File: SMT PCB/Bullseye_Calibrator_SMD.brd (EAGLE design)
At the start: 50.8 x 66 mm, 16 parts

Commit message: Add files via upload
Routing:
- net S$57: track 42.3 -> 33.8 mm, vias 2 -> 0
- net S$64: track 0.00 -> 8.26 mm
- net S$46: vias 1 -> 0
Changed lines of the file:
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@@
 <layer number="21" name="tPlace" color="7" fill="1" visible="yes" active="yes"/>
 <layer number="22" name="bPlace" color="7" fill="1" visible="yes" active="yes"/>
-<layer number="23" name="tOrigins" color="15" fill="1" visible="yes" active="yes"/>
-<layer number="24" name="bOrigins" color="15" fill="1" visible="yes" active="yes"/>
+<layer number="23" name="tOrigins" color="15" fill="1" visible="no" active="yes"/>
+<layer number="24" name="bOrigins" color="15" fill="1" visible="no" active="yes"/>
 <layer number="25" name="tNames" color="7" fill="1" visible="yes" active="yes"/>
 <layer number="26" name="bNames" color="7" fill="1" visible="yes" active="yes"/>
 <layer number="27" name="tValues" color="7" fill="1" visible="yes" active="yes"/>
 <layer number="28" name="bValues" color="7" fill="1" visible="yes" active="yes"/>
-<layer number="29" name="tStop" color="7" fill="3" visible="yes" active="yes"/>
-<layer number="30" name="bStop" color="7" fill="6" visible="yes" active="yes"/>
-<layer number="31" name="tCream" color="7" fill="4" visible="yes" active="yes"/>
-<layer number="32" name="bCream" color="7" fill="5" visible="yes" active="yes"/>
+<layer number="29" name="tStop" color="7" fill="3" visible="no" active="yes"/>
+<layer number="30" name="bStop" color="7" fill="6" visible="no" active="yes"/>
+<layer number="31" name="tCream" color="7" fill="4" visible="no" active="yes"/>
+<layer number="32" name="bCream" color="7" fill="5" visible="no" active="yes"/>
 <layer number="33" name="tFinish" color="6" fill="3" visible="yes" active="yes"/>
 <layer number="34" name="bFinish" color="6" fill="6" visible="yes" active="yes"/>
@@
 <wire x1="37.626753125" y1="43.18" x2="33.02" y2="43.18" width="0.8128" layer="1"/>
 </signal>
+<signal name="S$66">
+<wire x1="10.18568125" y1="35.56" x2="10.16" y2="35.56" width="1.778" layer="16"/>
+</signal>
 <signal name="S$46">
 <wire x1="43.6577875" y1="45.67815" x2="43.6577875" y2="39.2058875" width="1.4224" layer="1"/>
 <wire x1="43.6577875" y1="39.2058875" x2="10.18568125" y2="39.2058875" width="1.4224" layer="1"/>
 <wire x1="10.18568125" y1="39.2058875" x2="10.18568125" y2="35.56" width="1.4224" layer="1"/>
-<wire x1="10.18568125" y1="35.56" x2="10.16" y2="35.56" width="1.778" layer="16"/>
-<via x="10.18568125" y="35.56" extent="1-16" drill="0.6" shape="square"/>
-</signal>
-<signal name="S$57">
+</signal>
+<signal name="S$64">
 <wire x1="21.175271875" y1="54.165178125" x2="21.175271875" y2="62.4286" width="1.6764" layer="1"/>
+</signal>
+<signal name="S$65">
 <wire x1="21.175271875" y1="62.4286" x2="21.25105625" y2="62.4286" width="1.6764" layer="16"/>
 <wire x1="21.25105625" y1="62.4286" x2="21.25105625" y2="62.314884375" width="1.6764" layer="16"/>
+</signal>
+<signal name="S$57">
 <wire x1="21.25105625" y1="62.314884375" x2="29.246228125" y2="62.314884375" width="1.6764" layer="1"/>
 <wire x1="29.246228125" y1="62.314884375" x2="29.246228125" y2="54.09108125" width="1.6764" layer="1"/>
 <wire x1="29.246228125" y1="54.09108125" x2="43.2274" y2="54.09108125" width="1.4224" layer="1"/>
 <wire x1="43.2274" y1="54.09108125" x2="43.2274" y2="50.442665625" width="1.4224" layer="1"/>
-<via x="21.25105625" y="62.314884375" extent="1-16" drill="0.6" shape="square"/>
-<via x="21.175271875" y="62.4286" extent="1-16" drill="0.6" shape="square"/>
 </signal>
 <signal name="S$43">

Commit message: Add files via upload
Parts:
- added J3: (no value), jumper:JP1
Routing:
- net S$71: track 0.00 -> 29.6 mm
- net S$70: track 0.00 -> 24.5 mm
- net S$67: track 0.00 -> 16.2 mm
- net S$57: track 33.8 -> 23.1 mm
- net S$69: track 0.00 -> 8.06 mm
- net S$68: track 0.00 -> 3.07 mm
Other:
- board text added: "25 MHz Out"
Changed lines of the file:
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@@
 <layer number="21" name="tPlace" color="7" fill="1" visible="yes" active="yes"/>
 <layer number="22" name="bPlace" color="7" fill="1" visible="yes" active="yes"/>
-<layer number="23" name="tOrigins" color="15" fill="1" visible="no" active="yes"/>
-<layer number="24" name="bOrigins" color="15" fill="1" visible="no" active="yes"/>
+<layer number="23" name="tOrigins" color="15" fill="1" visible="yes" active="yes"/>
+<layer number="24" name="bOrigins" color="15" fill="1" visible="yes" active="yes"/>
 <layer number="25" name="tNames" color="7" fill="1" visible="yes" active="yes"/>
 <layer number="26" name="bNames" color="7" fill="1" visible="yes" active="yes"/>
 <layer number="27" name="tValues" color="7" fill="1" visible="yes" active="yes"/>
 <layer number="28" name="bValues" color="7" fill="1" visible="yes" active="yes"/>
-<layer number="29" name="tStop" color="7" fill="3" visible="no" active="yes"/>
-<layer number="30" name="bStop" color="7" fill="6" visible="no" active="yes"/>
-<layer number="31" name="tCream" color="7" fill="4" visible="no" active="yes"/>
-<layer number="32" name="bCream" color="7" fill="5" visible="no" active="yes"/>
+<layer number="29" name="tStop" color="7" fill="3" visible="yes" active="yes"/>
+<layer number="30" name="bStop" color="7" fill="6" visible="yes" active="yes"/>
+<layer number="31" name="tCream" color="7" fill="4" visible="yes" active="yes"/>
+<layer number="32" name="bCream" color="7" fill="5" visible="yes" active="yes"/>
 <layer number="33" name="tFinish" color="6" fill="3" visible="yes" active="yes"/>
 <layer number="34" name="bFinish" color="6" fill="6" visible="yes" active="yes"/>
@@
 G4EML</text>
 <text x="14.365821875" y="26.578703125" size="1.778" layer="21" font="fixed">ARDUINO NANO</text>
+<text x="42.65035" y="60.322175" size="1.778" layer="21" align="center">25
+MHz
+Out</text>
 </plain>
 <attributes>
@@
 <attribute name="VALUE" x="12.406625" y="49.139590625" size="1.27" layer="27" rot="R270"/>
 </element>
+<element name="J3" library="jumper" package="JP1" value="" x="46.93469375" y="59.850865625" smashed="yes">
+<attribute name="NAME" x="48.02838125" y="64.295721875" size="1.27" layer="25" ratio="10" rot="R180"/>
+<attribute name="VALUE" x="49.85569375" y="57.310865625" size="1.27" layer="27" ratio="10" rot="R90"/>
+</element>
 </elements>
 <signals>
@@
 <wire x1="21.25105625" y1="62.4286" x2="21.25105625" y2="62.314884375" width="1.6764" layer="16"/>
 </signal>
-<signal name="S$57">
+<signal name="S$67">
 <wire x1="21.25105625" y1="62.314884375" x2="29.246228125" y2="62.314884375" width="1.6764" layer="1"/>
 <wire x1="29.246228125" y1="62.314884375" x2="29.246228125" y2="54.09108125" width="1.6764" layer="1"/>
-<wire x1="29.246228125" y1="54.09108125" x2="43.2274" y2="54.09108125" width="1.4224" layer="1"/>
-<wire x1="43.2274" y1="54.09108125" x2="43.2274" y2="50.442665625" width="1.4224" layer="1"/>
+</signal>
+<signal name="S$57">
+<wire x1="29.246228125" y1="54.09108125" x2="43.7092375" y2="54.069178125" width="1.4224" layer="16"/>
+<wire x1="43.7092375" y1="54.069178125" x2="43.7358625" y2="45.4348" width="1.4224" layer="16"/>
 </signal>
 <signal name="S$43">
@@
 <wire x1="25.4" y1="48.6216125" x2="25.403265625" y2="48.6216125" width="0.8128" layer="1"/>
 </signal>
+<signal name="S$68">
+<wire x1="40.64594375" y1="50.511465625" x2="43.717578125" y2="50.511465625" width="1.4224" layer="16"/>
+</signal>
+<signal name="S$69">
+<wire x1="46.984446875" y1="58.63309375" x2="46.98445" y2="54.15151875" width="1.4224" layer="16"/>
+<wire x1="46.98445" y1="54.15151875" x2="43.411159375" y2="54.060634375" width="1.4224" layer="16"/>
+</signal>
+<signal name="S$70">
+<wire x1="29.198825" y1="54.139325" x2="29.198825" y2="62.30840625" width="1.6764" layer="16"/>
+<wire x1="29.198825" y1="62.30840625" x2="21.116028125" y2="62.30840625" width="1.6764" layer="16"/>
+<wire x1="21.116028125" y1="62.30840625" x2="21.116028125" y2="54.117425" width="1.6764" layer="16"/>
+<wire x1="21.116028125" y1="54.117425" x2="21.137934375" y2="54.117425" width="1.4224" layer="16"/>
+</signal>
+<signal name="S$71">
+<wire x1="29.894465625" y1="48.64216875" x2="29.894465625" y2="50.54755625" width="0.8128" layer="1"/>
+<wire x1="29.894465625" y1="50.54755625" x2="32.982465625" y2="50.54755625" width="0.8128" layer="1"/>
+<wire x1="32.982465625" y1="50.54755625" x2="32.982465625" y2="61.069878125" width="0.8128" layer="1"/>
+<wire x1="32.982465625" y1="61.069878125" x2="47.107109375" y2="61.06988125" width="0.8128" layer="1"/>
+</signal>
 </signals>

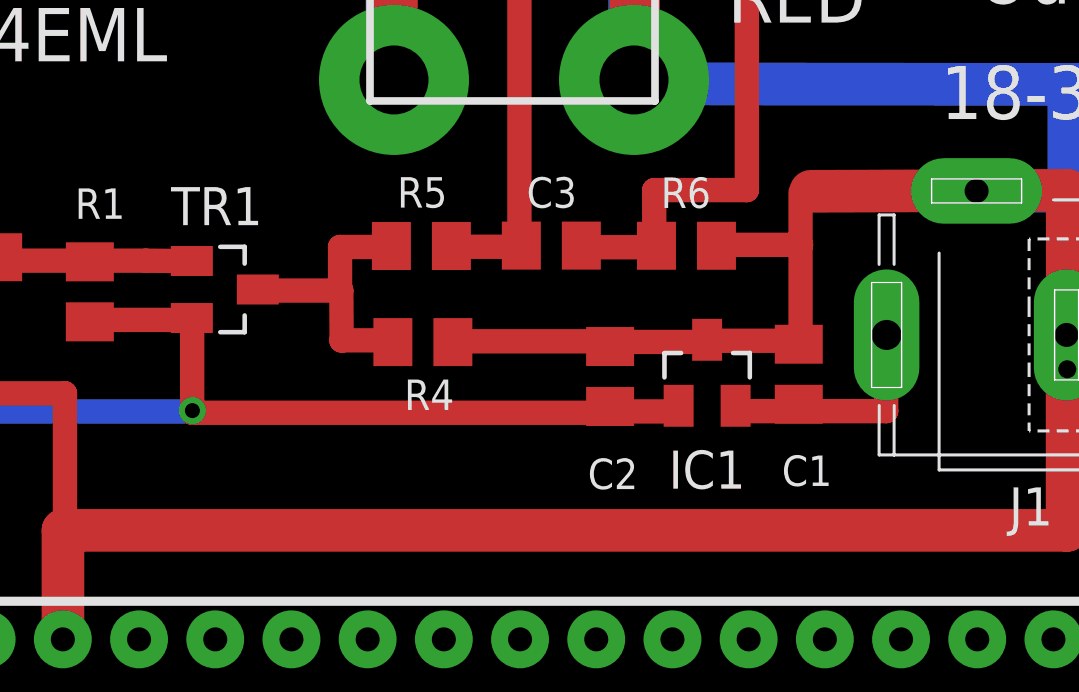
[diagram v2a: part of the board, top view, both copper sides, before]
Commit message: Add Input Diode
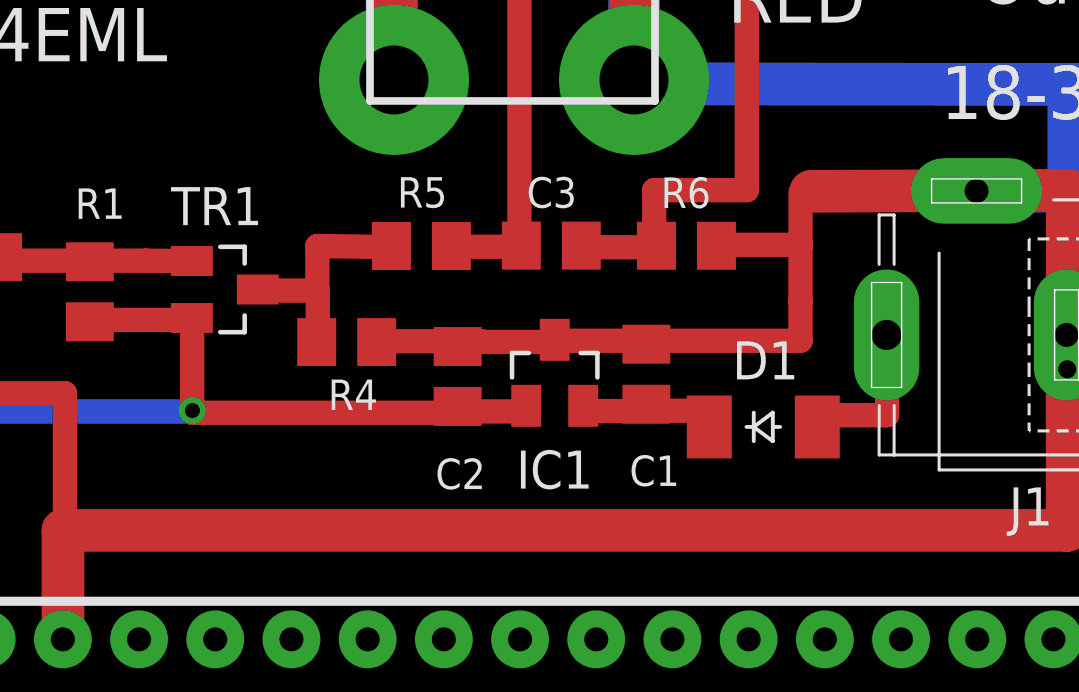
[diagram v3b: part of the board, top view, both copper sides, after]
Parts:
- added D1: (no value), diode:SOD-123_MINI-SMA
- moved C1 5.08 mm to (29.6, 44.4)
- moved C2 5.08 mm to (23.3, 44.3)
- moved IC1 5.08 mm to (26.6, 44.5)
- moved R4 2.54 mm to (19.6, 45.5)
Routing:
- net S$52: track 20.5 -> 15.5 mm
- net S$56: track 5.54 -> 0.46 mm
- net S$43: track 8.08 -> 13.2 mm
- net S$72: track 0.00 -> 4.58 mm
- net S$45: track 7.16 -> 3.97 mm
- net S$58: track 1.53 -> 3.16 mm
- net S$55: track 4.36 -> 3.57 mm
- net S$59: track 3.09 -> 3.85 mm
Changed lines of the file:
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@@
 <attribute name="VALUE" x="12.980653125" y="46.15735625" size="1.016" layer="27" rot="R90"/>
 </element>
-<element name="R4" library="resistor" package="C0805K" value="" x="22.182725" y="45.481446875" smashed="yes" rot="R180">
-<attribute name="NAME" x="23.22906875" y="44.235890625" size="1.016" layer="25" rot="R180"/>
-<attribute name="VALUE" x="23.182725" y="47.381446875" size="1.016" layer="27" rot="R180"/>
+<element name="R4" library="resistor" package="C0805K" value="" x="19.642725" y="45.481446875" smashed="yes" rot="R180">
+<attribute name="NAME" x="20.68906875" y="44.235890625" size="1.016" layer="25" rot="R180"/>
+<attribute name="VALUE" x="20.642725" y="47.381446875" size="1.016" layer="27" rot="R180"/>
 </element>
 <element name="R2" library="resistor" package="C0805K" value="" x="7.17551875" y="48.310884375" smashed="yes">
@@
 <attribute name="VALUE" x="6.98" y="39.64" size="1.016" layer="27" rot="R90"/>
 </element>
-<element name="C2" library="resistor" package="C0805K" value="" x="28.4231375" y="44.334334375" smashed="yes" rot="R90">
-<attribute name="NAME" x="29.352946875" y="41.598025" size="1.016" layer="25" rot="R180"/>
-<attribute name="VALUE" x="30.3231375" y="43.334334375" size="1.016" layer="27" rot="R90"/>
-</element>
-<element name="C1" library="resistor" package="C0805K" value="" x="34.712721875" y="44.41035625" smashed="yes" rot="R90">
-<attribute name="NAME" x="35.8213625" y="41.70223125" size="1.016" layer="25" rot="R180"/>
-<attribute name="VALUE" x="36.612721875" y="43.41035625" size="1.016" layer="27" rot="R90"/>
-</element>
-<element name="IC1" library="avago" package="SOT23" value="" x="31.65776875" y="44.457725" smashed="yes">
-<attribute name="NAME" x="30.377315625" y="40.59605625" size="1.27" layer="25"/>
-<attribute name="VALUE" x="29.75276875" y="41.282725" size="1.27" layer="27"/>
+<element name="C2" library="resistor" package="C0805K" value="" x="23.3431375" y="44.334334375" smashed="yes" rot="R90">
+<attribute name="NAME" x="24.272946875" y="41.598025" size="1.016" layer="25" rot="R180"/>
+<attribute name="VALUE" x="25.2431375" y="43.334334375" size="1.016" layer="27" rot="R90"/>
+</element>
+<element name="C1" library="resistor" package="C0805K" value="" x="29.632721875" y="44.41035625" smashed="yes" rot="R90">
+<attribute name="NAME" x="30.7413625" y="41.70223125" size="1.016" layer="25" rot="R180"/>
+<attribute name="VALUE" x="31.532721875" y="43.41035625" size="1.016" layer="27" rot="R90"/>
+</element>
+<element name="IC1" library="avago" package="SOT23" value="" x="26.57776875" y="44.457725" smashed="yes">
+<attribute name="NAME" x="25.297315625" y="40.59605625" size="1.27" layer="25"/>
+<attribute name="VALUE" x="24.67276875" y="41.282725" size="1.27" layer="27"/>
 </element>
 <element name="TR2" library="avago" package="SOT23" value="" x="6.06380625" y="44.914759375" smashed="yes">
@@
 <attribute name="NAME" x="48.02838125" y="64.295721875" size="1.27" layer="25" ratio="10" rot="R180"/>
 <attribute name="VALUE" x="49.85569375" y="57.310865625" size="1.27" layer="27" ratio="10" rot="R90"/>
+</element>
+<element name="D1" library="diode" package="SOD-123_MINI-SMA" value="" x="33.529925" y="42.65389375" smashed="yes">
+<attribute name="NAME" x="32.500659375" y="44.238575" size="1.27" layer="25"/>
+<attribute name="VALUE" x="30.481925" y="40.24089375" size="1.27" layer="27"/>
 </element>
 </elements>
@@
 </signal>
 <signal name="S$45">
-<wire x1="37.626753125" y1="45.73158125" x2="37.626753125" y2="43.18" width="0.8128" layer="1"/>
-<wire x1="37.626753125" y1="43.18" x2="33.02" y2="43.18" width="0.8128" layer="1"/>
+<wire x1="31.913771875" y1="43.198246875" x2="27.94" y2="43.18" width="0.8128" layer="1"/>
 </signal>
 <signal name="S$66">
@@
 </signal>
 <signal name="S$43">
-<wire x1="31.64364375" y1="45.525934375" x2="34.771325" y2="45.525934375" width="0.8128" layer="1"/>
-<wire x1="34.771325" y1="45.525934375" x2="34.771325" y2="50.47855625" width="0.8128" layer="1"/>
+<wire x1="26.56364375" y1="45.525934375" x2="34.770703125" y2="45.525934375" width="0.8128" layer="1"/>
+<wire x1="34.770703125" y1="45.525934375" x2="34.770703125" y2="46.839978125" width="0.8128" layer="1"/>
+<wire x1="34.770703125" y1="46.839978125" x2="34.771325" y2="50.47855625" width="0.8128" layer="1"/>
 </signal>
 <signal name="S$47">
-<wire x1="31.717871875" y1="45.4873375" x2="28.300915625" y2="45.4873375" width="0.8128" layer="1"/>
+<wire x1="26.637871875" y1="45.4873375" x2="23.220915625" y2="45.4873375" width="0.8128" layer="1"/>
 </signal>
 <signal name="S$48">
-<wire x1="30.6754125" y1="43.171478125" x2="28.455353125" y2="43.171478125" width="0.8128" layer="1"/>
-<wire x1="28.455353125" y1="43.171478125" x2="28.455353125" y2="43.152178125" width="0.8128" layer="1"/>
+<wire x1="25.5954125" y1="43.171478125" x2="23.375353125" y2="43.171478125" width="0.8128" layer="1"/>
+<wire x1="23.375353125" y1="43.171478125" x2="23.375353125" y2="43.152178125" width="0.8128" layer="1"/>
 </signal>
 <signal name="S$34">
@@
 <wire x1="11.099271875" y1="46.221234375" x2="14.493153125" y2="46.221234375" width="0.8128" layer="1"/>
 <wire x1="14.493153125" y1="46.221234375" x2="14.493153125" y2="43.1259125" width="0.8128" layer="1"/>
-<wire x1="14.493153125" y1="43.1259125" x2="28.50586875" y2="43.1259125" width="0.8128" layer="1"/>
-<wire x1="28.50586875" y1="43.1259125" x2="28.50586875" y2="43.165953125" width="0.8128" layer="1"/>
+<wire x1="14.493153125" y1="43.1259125" x2="23.42586875" y2="43.1259125" width="0.8128" layer="1"/>
+<wire x1="23.42586875" y1="43.1259125" x2="23.42586875" y2="43.165953125" width="0.8128" layer="1"/>
 </signal>
 <signal name="S$53">
@@
 </signal>
 <signal name="S$55">
-<wire x1="16.775975" y1="47.199303125" x2="19.4638375" y2="47.199303125" width="0.8128" layer="1"/>
-<wire x1="19.4638375" y1="47.199303125" x2="19.475003125" y2="45.530175" width="0.8128" layer="1"/>
+<wire x1="16.775975" y1="47.199303125" x2="18.67516875" y2="47.199303125" width="0.8128" layer="1"/>
+<wire x1="18.67516875" y1="47.199303125" x2="18.686334375" y2="45.530175" width="0.8128" layer="1"/>
 </signal>
 <signal name="S$56">
-<wire x1="23.2327375" y1="45.508721875" x2="28.512196875" y2="45.50871875" width="0.8128" layer="1"/>
-<wire x1="28.512196875" y1="45.50871875" x2="28.454278125" y2="45.25389375" width="0.8128" layer="1"/>
+<wire x1="23.2327375" y1="45.508721875" x2="23.432196875" y2="45.50871875" width="0.8128" layer="1"/>
+<wire x1="23.432196875" y1="45.50871875" x2="23.374278125" y2="45.25389375" width="0.8128" layer="1"/>
 </signal>
 <signal name="S$58">
-<wire x1="19.462446875" y1="45.540190625" x2="20.990490625" y2="45.540190625" width="0.8128" layer="1"/>
+<wire x1="24.146146875" y1="45.509778125" x2="20.990490625" y2="45.509778125" width="0.8128" layer="1"/>
 </signal>
 <signal name="S$59">
-<wire x1="19.42208125" y1="47.147034375" x2="19.42208125" y2="48.65234375" width="0.8128" layer="1"/>
-<wire x1="19.42208125" y1="48.65234375" x2="21.00519375" y2="48.65234375" width="0.8128" layer="1"/>
+<wire x1="18.664959375" y1="47.178584375" x2="18.664959375" y2="48.68389375" width="0.8128" layer="1"/>
+<wire x1="18.664959375" y1="48.68389375" x2="21.00519375" y2="48.65234375" width="0.8128" layer="1"/>
 </signal>
 <signal name="S$60">
@@
 <wire x1="32.982465625" y1="61.069878125" x2="47.107109375" y2="61.06988125" width="0.8128" layer="1"/>
 </signal>
+<signal name="S$72">
+<wire x1="35.701571875" y1="43.04460625" x2="37.654575" y2="43.04460625" width="0.8128" layer="1"/>
+<wire x1="37.654575" y1="43.04460625" x2="37.654575" y2="45.672171875" width="0.8128" layer="1"/>
+</signal>
 </signals>
